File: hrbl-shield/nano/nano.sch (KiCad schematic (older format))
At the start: 61 parts, among them P1 Digital, P2 Analog, P3 CONN_01X01, P4 CONN_01X01, P5 CONN_01X01, P6 CONN_01X01, U1 SFH6206-3T, U10 SFH6206-3T, U11 SFH6206-3T, U12 SFH6206-3T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

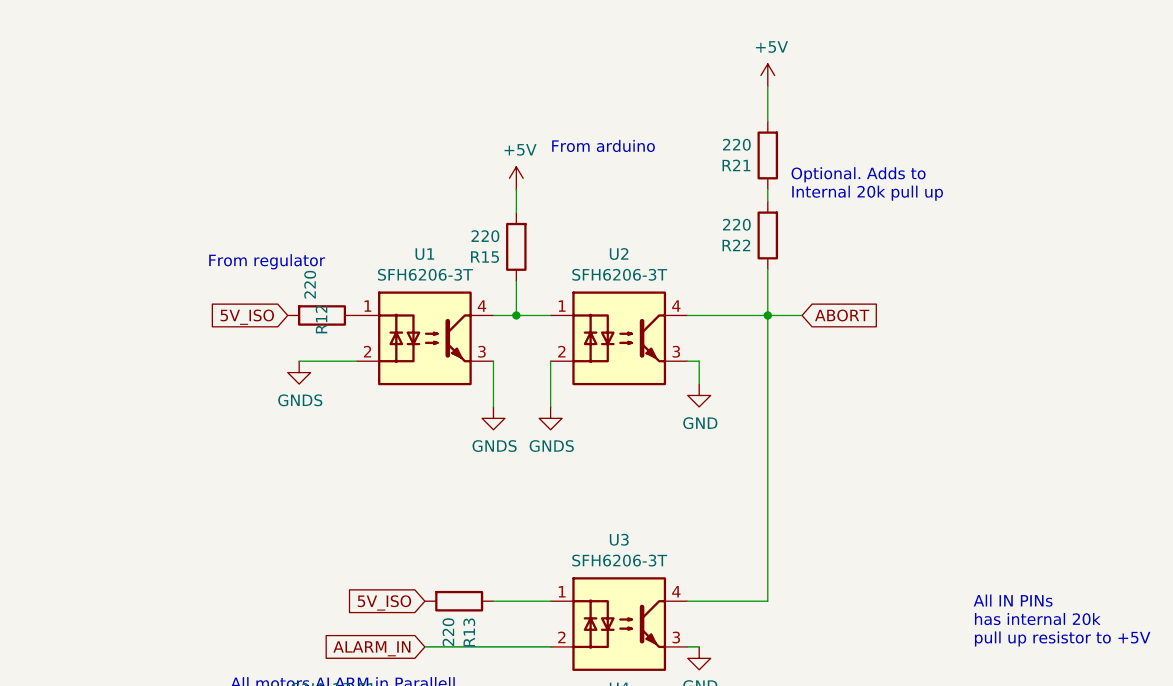
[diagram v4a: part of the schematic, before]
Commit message: Hrbl with abort function (needs patch cable)
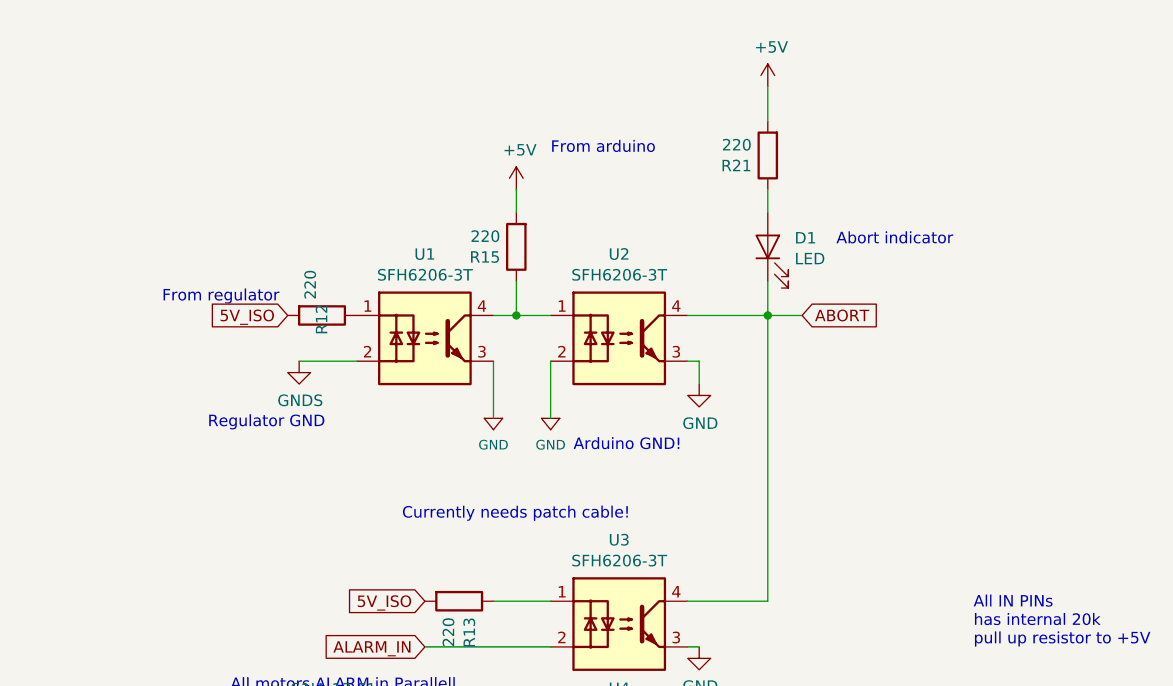
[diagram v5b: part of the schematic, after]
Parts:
- removed R22: 220, Resistor_SMD:R_1206_3216Metric_Pad1.42x1.75mm_HandSolder, symbol Device:R
- added D1: LED, LED_SMD:LED_1206_3216Metric_Pad1.42x1.75mm_HandSolder, symbol Device:LED
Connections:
- net ABORT: now also D1.1 (K)
- net GNDS: no longer U1.3, U2.2
- net at R21.1: now also D1.2 (A)
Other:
- note added: "Abort indicator"
- note added: "Arduino GND!"
- note added: "Currently needs patch cable!"
- note added: "Regulator GND"
- note removed: "Optional. Adds to\nInternal 20k pull up"
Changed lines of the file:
@@
 	-1   0    0    1
-$EndComp
-$Comp
-L power:GNDS #PWR08
-U 1 1 5B9C09BB
-P 1500 2400
-F 0 "#PWR08" H 1500 2150 50  0001 C CNN
-F 1 "GNDS" H 1505 2227 50  0000 C CNN
-F 2 "" H 1500 2400 50  0001 C CNN
-F 3 "" H 1500 2400 50  0001 C CNN
-	1    1500 2400
-	1    0    0    -1
 $EndComp
 Text Notes 350  3650 0    50   ~ 0
@@
 	1    0    0    -1
 $EndComp
-$Comp
-L power:GNDS #PWR0116
-U 1 1 5B98D457
-P 1750 2400
-F 0 "#PWR0116" H 1750 2150 50  0001 C CNN
-F 1 "GNDS" H 1755 2227 50  0000 C CNN
-F 2 "" H 1750 2400 50  0001 C CNN
-F 3 "" H 1750 2400 50  0001 C CNN
-	1    1750 2400
-	1    0    0    -1
-$EndComp
 Wire Wire Line
 	1600 1850 1600 2000
@@
 	1    0    0    -1
 $EndComp
-$Comp
-L Device:R R22
-U 1 1 5B9E16EA
-P 2700 1650
-F 0 "R22" H 2770 1696 50  0000 L CNN
-F 1 "220" H 2770 1605 50  0000 L CNN
-F 2 "Resistor_SMD:R_1206_3216Metric_Pad1.42x1.75mm_HandSolder" V 2630 1650 50  0001 C CNN
-F 3 "~" H 2700 1650 50  0001 C CNN
-	1    2700 1650
-	-1   0    0    1
-$EndComp
 Wire Wire Line
 	2700 1000 2700 1150
-Wire Wire Line
-	2700 1450 2700 1500
-Wire Wire Line
-	2700 1800 2700 2000
-Text Notes 2800 1500 0    50   ~ 0
-Optional. Adds to\nInternal 20k pull up
-Text Notes 250  1800 0    50   ~ 0
+Text Notes 50   1950 0    50   ~ 0
 From regulator
 Text Notes 1750 1300 0    50   ~ 0
@@
 Wire Wire Line
 	2700 2000 2700 3250
-Wire Wire Line
-	1500 2200 1500 2400
 $Comp
 L pspice:DIODE S1JA-13-F2
@@
 Wire Wire Line
 	1150 5200 1000 5200
-Wire Wire Line
-	1750 2400 1750 2200
 $Comp
 L power:PWR_FLAG #FLG0105
@@
 Wire Wire Line
 	1450 4550 1750 4550
+$Comp
+L Device:LED D1
+U 1 1 5B996CA3
+P 2700 1700
+F 0 "D1" V 2738 1583 50  0000 R CNN
+F 1 "LED" V 2647 1583 50  0000 R CNN
+F 2 "LED_SMD:LED_1206_3216Metric_Pad1.42x1.75mm_HandSolder" H 2700 1700 50  0001 C CNN
+F 3 "~" H 2700 1700 50  0001 C CNN
+	1    2700 1700
+	0    -1   -1   0
+$EndComp
+Wire Wire Line
+	2700 1450 2700 1550
+Wire Wire Line
+	2700 1850 2700 2000
+Text Notes 3000 1700 0    50   ~ 0
+Abort indicator
+$Comp
+L nano-eagle-import:GND #SUPPLY01
+U 1 1 5B9CDDAB
+P 1750 2450
+F 0 "#SUPPLY01" H 1750 2450 50  0001 C CNN
+F 1 "GND" H 1750 2333 42  0000 C CNN
+F 2 "" H 1750 2450 50  0001 C CNN
+F 3 "" H 1750 2450 50  0001 C CNN
+	1    1750 2450
+	1    0    0    -1
+$EndComp
+$Comp
+L nano-eagle-import:GND #SUPPLY0101
+U 1 1 5B9D63D9
+P 1500 2450
+F 0 "#SUPPLY0101" H 1500 2450 50  0001 C CNN
+F 1 "GND" H 1500 2333 42  0000 C CNN
+F 2 "" H 1500 2450 50  0001 C CNN
+F 3 "" H 1500 2450 50  0001 C CNN
+	1    1500 2450
+	1    0    0    -1
+$EndComp
+Wire Wire Line
+	1750 2200 1750 2450
+Wire Wire Line
+	1500 2200 1500 2450
+Text Notes 1100 2900 0    50   ~ 0
+Currently needs patch cable!
+Text Notes 1850 2600 0    50   ~ 0
+Arduino GND!
+Text Notes 250  2500 0    50   ~ 0
+Regulator GND
 $EndSCHEMATC

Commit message: Removed the need for patch cable
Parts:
- added R22: 0, Resistor_SMD:R_1206_3216Metric_Pad1.42x1.75mm_HandSolder, symbol Device:R
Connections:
- net at U2.2: now also R22.1, R22.2
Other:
- note removed: "Currently needs patch cable!"
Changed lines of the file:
@@
 L power:GND #PWR04
 U 1 1 5B83CE76
-P 6150 6150
-F 0 "#PWR04" H 6150 5900 50  0001 C CNN
-F 1 "GND" H 6155 5977 50  0000 C CNN
-F 2 "" H 6150 6150 50  0001 C CNN
-F 3 "" H 6150 6150 50  0001 C CNN
-	1    6150 6150
+P 5950 6250
+F 0 "#PWR04" H 5950 6000 50  0001 C CNN
+F 1 "GND" H 5955 6077 50  0000 C CNN
+F 2 "" H 5950 6250 50  0001 C CNN
+F 3 "" H 5950 6250 50  0001 C CNN
+	1    5950 6250
 	1    0    0    -1
 $EndComp
@@
 L nano-eagle-import:GND #SUPPLY01
 U 1 1 5B9CDDAB
-P 1750 2450
-F 0 "#SUPPLY01" H 1750 2450 50  0001 C CNN
-F 1 "GND" H 1750 2333 42  0000 C CNN
-F 2 "" H 1750 2450 50  0001 C CNN
-F 3 "" H 1750 2450 50  0001 C CNN
-	1    1750 2450
+P 1750 2650
+F 0 "#SUPPLY01" H 1750 2650 50  0001 C CNN
+F 1 "GND" H 1750 2533 42  0000 C CNN
+F 2 "" H 1750 2650 50  0001 C CNN
+F 3 "" H 1750 2650 50  0001 C CNN
+	1    1750 2650
 	1    0    0    -1
 $EndComp
@@
 L nano-eagle-import:GND #SUPPLY0101
 U 1 1 5B9D63D9
-P 1500 2450
-F 0 "#SUPPLY0101" H 1500 2450 50  0001 C CNN
-F 1 "GND" H 1500 2333 42  0000 C CNN
-F 2 "" H 1500 2450 50  0001 C CNN
-F 3 "" H 1500 2450 50  0001 C CNN
-	1    1500 2450
-	1    0    0    -1
-$EndComp
-Wire Wire Line
-	1750 2200 1750 2450
-Wire Wire Line
-	1500 2200 1500 2450
-Text Notes 1100 2900 0    50   ~ 0
-Currently needs patch cable!
-Text Notes 1850 2600 0    50   ~ 0
+P 1500 2650
+F 0 "#SUPPLY0101" H 1500 2650 50  0001 C CNN
+F 1 "GND" H 1500 2533 42  0000 C CNN
+F 2 "" H 1500 2650 50  0001 C CNN
+F 3 "" H 1500 2650 50  0001 C CNN
+	1    1500 2650
+	1    0    0    -1
+$EndComp
+Text Notes 2550 2500 0    50   ~ 0
 Arduino GND!
 Text Notes 250  2500 0    50   ~ 0
 Regulator GND
+$Comp
+L Device:R R22
+U 1 1 5BA17A51
+P 2100 2550
+F 0 "R22" H 2030 2504 50  0000 R CNN
+F 1 "0" H 2030 2595 50  0000 R CNN
+F 2 "Resistor_SMD:R_1206_3216Metric_Pad1.42x1.75mm_HandSolder" V 2030 2550 50  0001 C CNN
+F 3 "~" H 2100 2550 50  0001 C CNN
+	1    2100 2550
+	-1   0    0    1
+$EndComp
+Wire Wire Line
+	6150 6150 5950 6150
+Wire Wire Line
+	5950 6150 5950 6250
+Wire Wire Line
+	1500 2200 1500 2650
+Wire Wire Line
+	2100 2400 1750 2400
+Wire Wire Line
+	1750 2200 1750 2400
+Wire Wire Line
+	2100 2700 1900 2700
+Wire Wire Line
+	1900 2700 1900 2550
+Wire Wire Line
+	1900 2550 1750 2550
+Wire Wire Line
+	1750 2550 1750 2650
+Connection ~ 1750 2550
+Connection ~ 1750 2400
+Wire Wire Line
+	1750 2400 1750 2550
 $EndSCHEMATC

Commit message: Corrected value
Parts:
- added C4: 100nF (0.1uF), Capacitor_SMD:C_1206_3216Metric_Pad1.42x1.75mm_HandSolder, symbol pspice:CAP
- added C5, C6: 10uF, Capacitor_SMD:C_1206_3216Metric_Pad1.42x1.75mm_HandSolder, symbol pspice:CAP
- added R23, R24, R25, R26: 1000, Resistor_SMD:R_1206_3216Metric_Pad1.42x1.75mm_HandSolder, symbol Device:R
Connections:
- net +36V: now also C5.1
- net +5V: now also C6.2, R23.1, R24.1, R25.1, R26.1
- net GND: now also C6.1
- net GNDPWR: now also C5.2
- net GNDS: now also C4.2
- net LIM_X: now also R23.2
- net LIM_Y: now also R24.2
- net LIM_Z: now also R25.2
- net PROBE: now also R26.2
- net VI: now also C4.1
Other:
- moved on the sheet: C1, C2

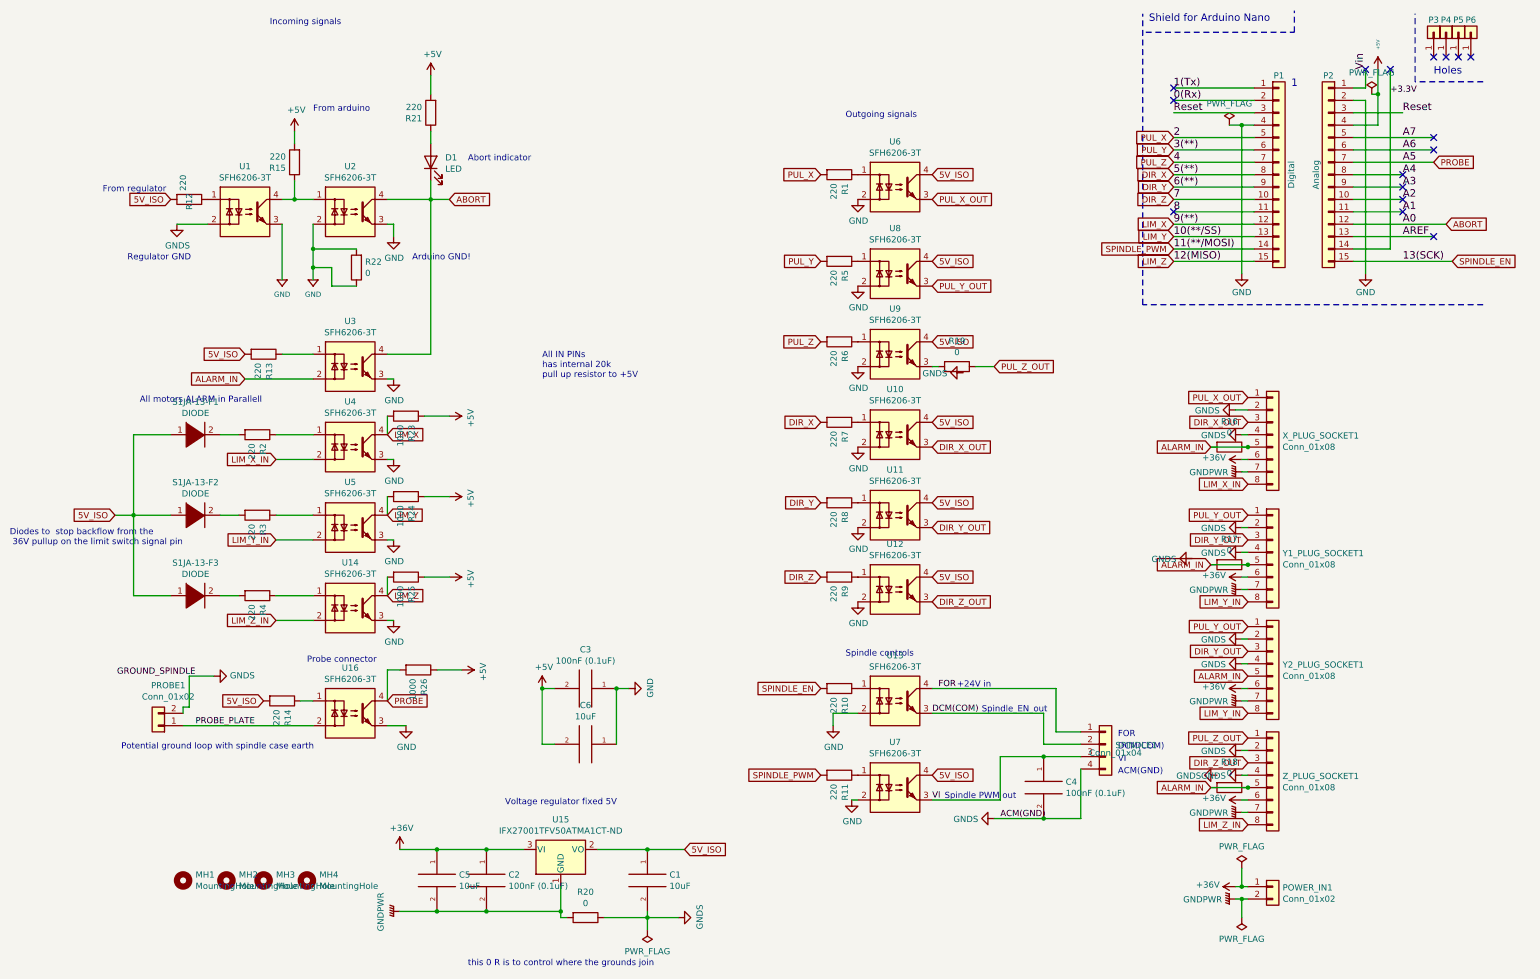
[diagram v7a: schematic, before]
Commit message: Fixes to 8pin connector version. Can now be archived.
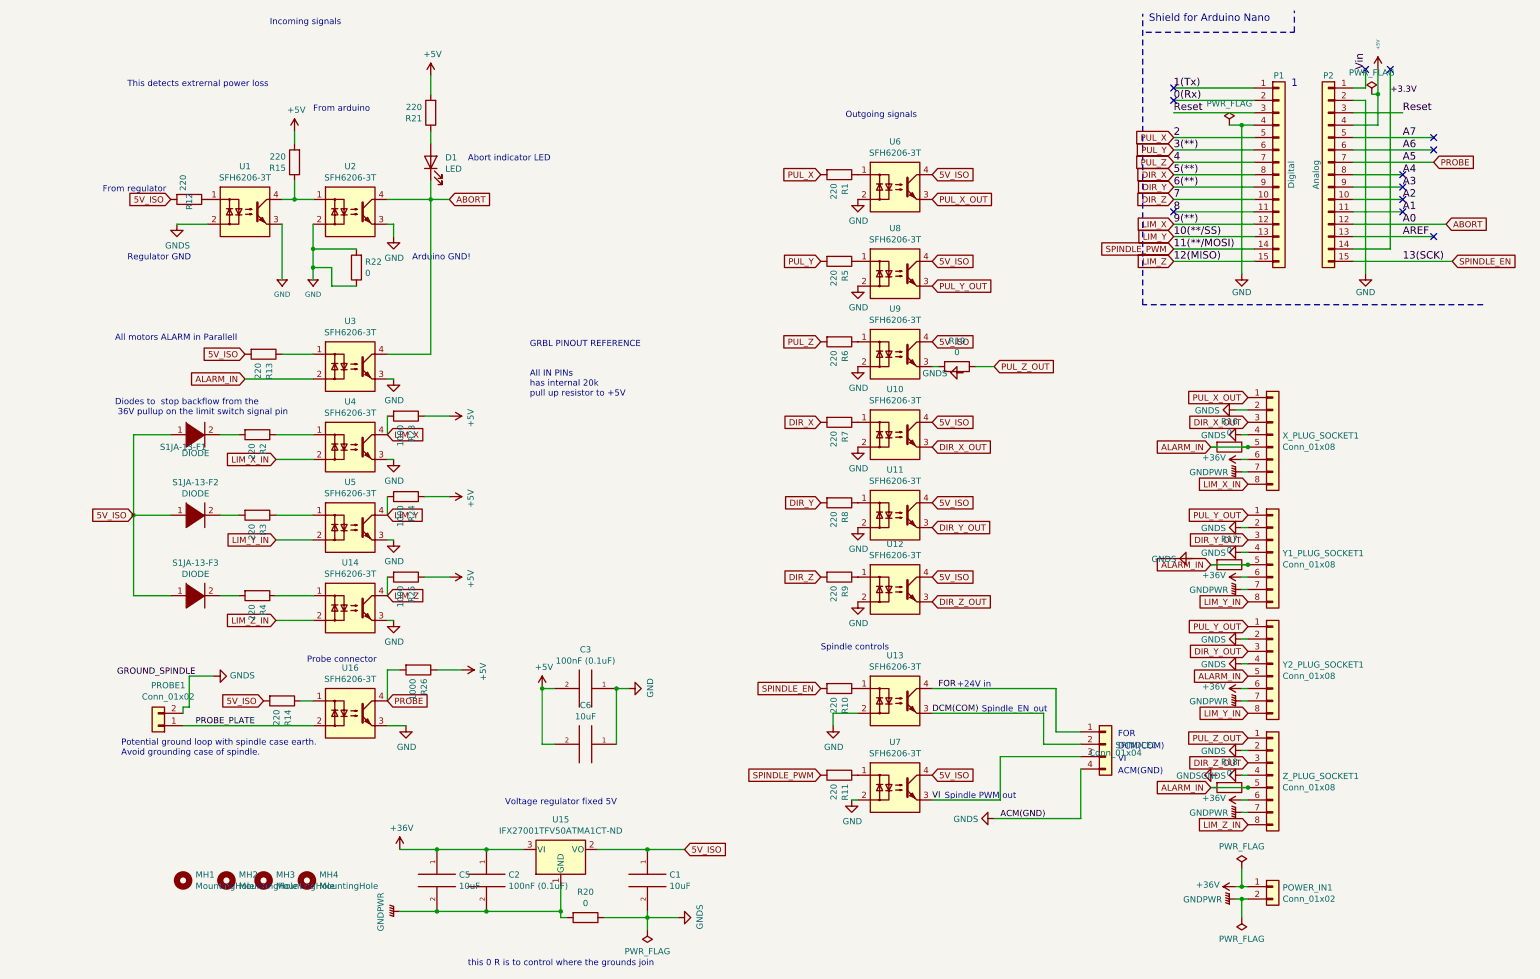
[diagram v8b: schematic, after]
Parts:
- removed C4: 100nF (0.1uF), Capacitor_SMD:C_1206_3216Metric_Pad1.42x1.75mm_HandSolder, symbol pspice:CAP
- removed P3, P4, P5, P6: CONN_01X01, Socket_Arduino_Nano:1pin_Nano, symbol Connector_Generic:Conn_01x01
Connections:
- no-connect marks 16 -> 12
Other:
- note added: "Abort indicator LED"
- note added: "GRBL PINOUT REFERENCE"
- note added: "Potential ground loop with spindle case earth. \nAvoid grounding case of spindle."
- note added: "This detects extrernal power loss"
- note removed: "Abort indicator"
- note removed: "Holes"
- note removed: "Potential ground loop with spindle case earth"
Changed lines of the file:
@@
 Text Label 10550 1300 0    60   ~ 0
 Reset
-Text Notes 10800 1000 0    60   ~ 0
-Holes
 Text Notes 8500 575  0    60   ~ 0
 Shield for Arduino Nano
@@
 	9675 650  9675 475
 $Comp
-L Connector_Generic:Conn_01x01 P3
-U 1 1 56D73ADD
-P 10800 650
-F 0 "P3" V 10900 650 50  0000 C CNN
-F 1 "CONN_01X01" V 10900 650 50  0001 C CNN
-F 2 "Socket_Arduino_Nano:1pin_Nano" H 10800 650 50  0001 C CNN
-F 3 "" H 10800 650 50  0000 C CNN
-	1    10800 650
-	0    -1   -1   0
-$EndComp
-NoConn ~ 10800 850
-$Comp
-L Connector_Generic:Conn_01x01 P4
-U 1 1 56D73D86
-P 10900 650
-F 0 "P4" V 11000 650 50  0000 C CNN
-F 1 "CONN_01X01" V 11000 650 50  0001 C CNN
-F 2 "Socket_Arduino_Nano:1pin_Nano" H 10900 650 50  0001 C CNN
-F 3 "" H 10900 650 50  0000 C CNN
-	1    10900 650
-	0    -1   -1   0
-$EndComp
-$Comp
-L Connector_Generic:Conn_01x01 P5
-U 1 1 56D73DAE
-P 11000 650
-F 0 "P5" V 11100 650 50  0000 C CNN
-F 1 "CONN_01X01" V 11100 650 50  0001 C CNN
-F 2 "Socket_Arduino_Nano:1pin_Nano" H 11000 650 50  0001 C CNN
-F 3 "" H 11000 650 50  0000 C CNN
-	1    11000 650
-	0    -1   -1   0
-$EndComp
-$Comp
-L Connector_Generic:Conn_01x01 P6
-U 1 1 56D73DD9
-P 11100 650
-F 0 "P6" V 11200 650 50  0000 C CNN
-F 1 "CONN_01X01" V 11200 650 50  0001 C CNN
-F 2 "Socket_Arduino_Nano:1pin_Nano" H 11100 650 50  0001 C CNN
-F 3 "" H 11100 650 50  0000 C CNN
-	1    11100 650
-	0    -1   -1   0
-$EndComp
-NoConn ~ 10900 850
-NoConn ~ 11000 850
-NoConn ~ 11100 850
-$Comp
 L Connector_Generic:Conn_01x15 P1
 U 1 1 56D73FAC
@@
 	10550 1300 10150 1300
 Wire Notes Line
-	11200 1050 10650 1050
-Wire Notes Line
-	10650 1050 10650 500
-Wire Notes Line
 	11200 2850 8450 2850
 Wire Notes Line
@@
 	1    0    0    -1
 $EndComp
-Text Notes 6050 5700 0    50   ~ 0
+Text Notes 5850 5650 0    50   ~ 0
 Spindle controls
 $Comp
@@
 Text GLabel 6750 1800 2    50   Input ~ 0
 5V_ISO
-Text GLabel 150  4550 0    50   Input ~ 0
+Text GLabel 300  4550 0    50   Input ~ 0
 5V_ISO
 Text GLabel 4750 7250 2    50   Input ~ 0
@@
 Text GLabel 2850 2000 2    50   Input ~ 0
 ABORT
-Text Notes 3600 3450 0    50   ~ 0
+Text Notes 3500 3600 0    50   ~ 0
 All IN PINs\nhas internal 20k \npull up resistor to +5V
 $Comp
@@
 	-1   0    0    1
 $EndComp
-Text Notes 350  3650 0    50   ~ 0
+Text Notes 150  3150 0    50   ~ 0
 All motors ALARM in Parallell
-Text Notes 200  6450 0    50   ~ 0
-Potential ground loop with spindle case earth
 Wire Wire Line
 	9200 7550 9250 7550
@@
 U 1 1 5B92F59F
 P 800 3900
-F 0 "S1JA-13-F1" H 800 4165 50  0000 C CNN
-F 1 "DIODE" H 800 4074 50  0000 C CNN
+F 0 "S1JA-13-F1" H 700 3800 50  0000 C CNN
+F 1 "DIODE" H 800 3750 50  0000 C CNN
 F 2 "Diode_SMD:D_SMA_Handsoldering" H 800 3900 50  0001 C CNN
 F 3 "https://www.diodes.com/assets/Datasheets/ds16003.pdf" H 800 3900 50  0001 C CNN
@@
 	0    1    1    0
 $EndComp
-Text Notes -700 4800 0    50   ~ 0
+Text Notes 150  3750 0    50   ~ 0
 Diodes to  stop backflow from the\n 36V pullup on the limit switch signal pin
 Text Notes 1400 600  0    50   ~ 0
@@
 	300  4550 300  5200
 Wire Wire Line
-	150  4550 300  4550
-Wire Wire Line
 	1000 3900 1150 3900
 Wire Wire Line
@@
 	2700 1850 2700 2000
 Text Notes 3000 1700 0    50   ~ 0
-Abort indicator
+Abort indicator LED
 $Comp
 L nano-eagle-import:GND #SUPPLY01
@@
 Wire Wire Line
 	1750 2400 1750 2550
-$Comp
-L pspice:CAP C4
-U 1 1 5BB54227
-P 7650 6750
-F 0 "C4" H 7828 6796 50  0000 L CNN
-F 1 "100nF (0.1uF)" H 7828 6705 50  0000 L CNN
-F 2 "Capacitor_SMD:C_1206_3216Metric_Pad1.42x1.75mm_HandSolder" H 7650 6750 50  0001 C CNN
-F 3 "" H 7650 6750 50  0001 C CNN
-	1    7650 6750
-	1    0    0    -1
-$EndComp
-Wire Wire Line
-	7950 6500 7650 6500
 Wire Wire Line
 	7950 6600 7950 7000
 Wire Wire Line
-	7950 7000 7650 7000
-Wire Wire Line
-	7650 6500 7300 6500
-Wire Wire Line
 	7300 6500 7300 6850
 Wire Wire Line
 	7300 6850 6750 6850
-Connection ~ 7650 6500
-Wire Wire Line
-	7650 7000 7250 7000
-Connection ~ 7650 7000
 $Comp
 L power:+5V #PWR037
@@
 Connection ~ 2750 7750
 Connection ~ 3150 7750
+Text Notes 250  1100 0    50   ~ 0
+This detects extrernal power loss
+Text Notes 200  6500 0    50   ~ 0
+Potential ground loop with spindle case earth. \nAvoid grounding case of spindle.
+Wire Wire Line
+	7300 6500 7950 6500
+Wire Wire Line
+	7250 7000 7950 7000
+Text Notes 3500 3200 0    50   ~ 0
+GRBL PINOUT REFERENCE
 $EndSCHEMATC
